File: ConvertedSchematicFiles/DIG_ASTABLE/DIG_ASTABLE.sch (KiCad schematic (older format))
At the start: 11 parts, among them U1 7404, U4 7400

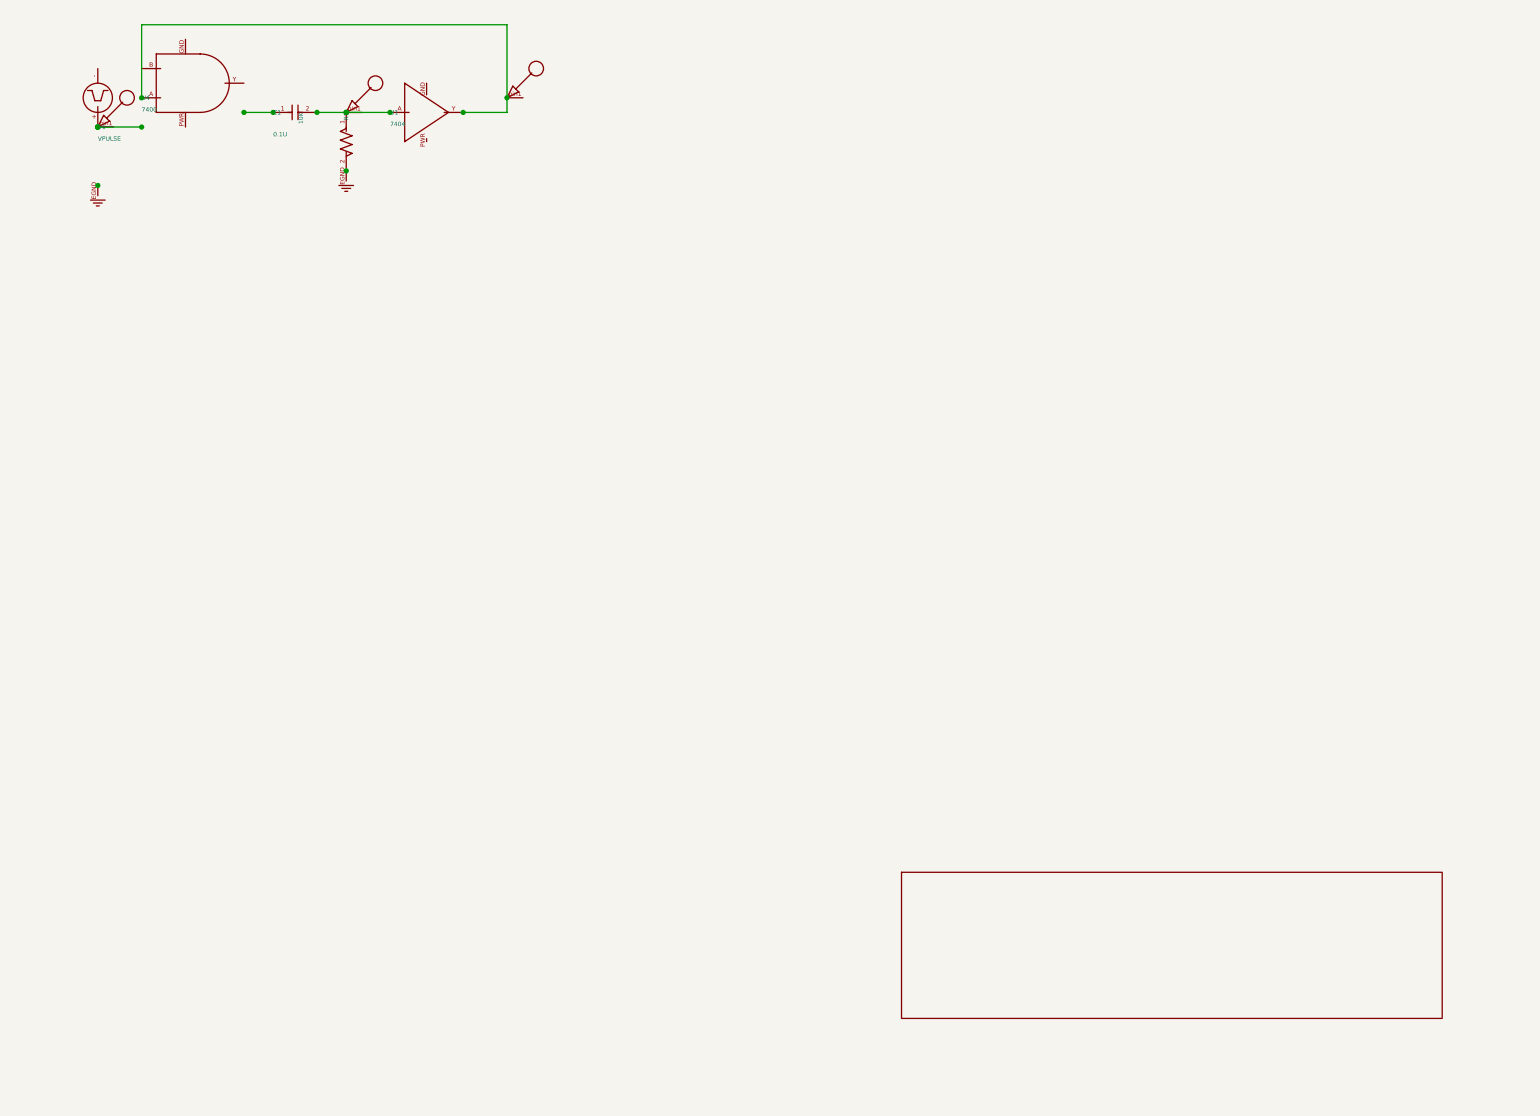
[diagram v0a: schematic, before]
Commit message: Excluded some components. These no longer appear after conversion. When calling shell commands, filenames are in "quotes"
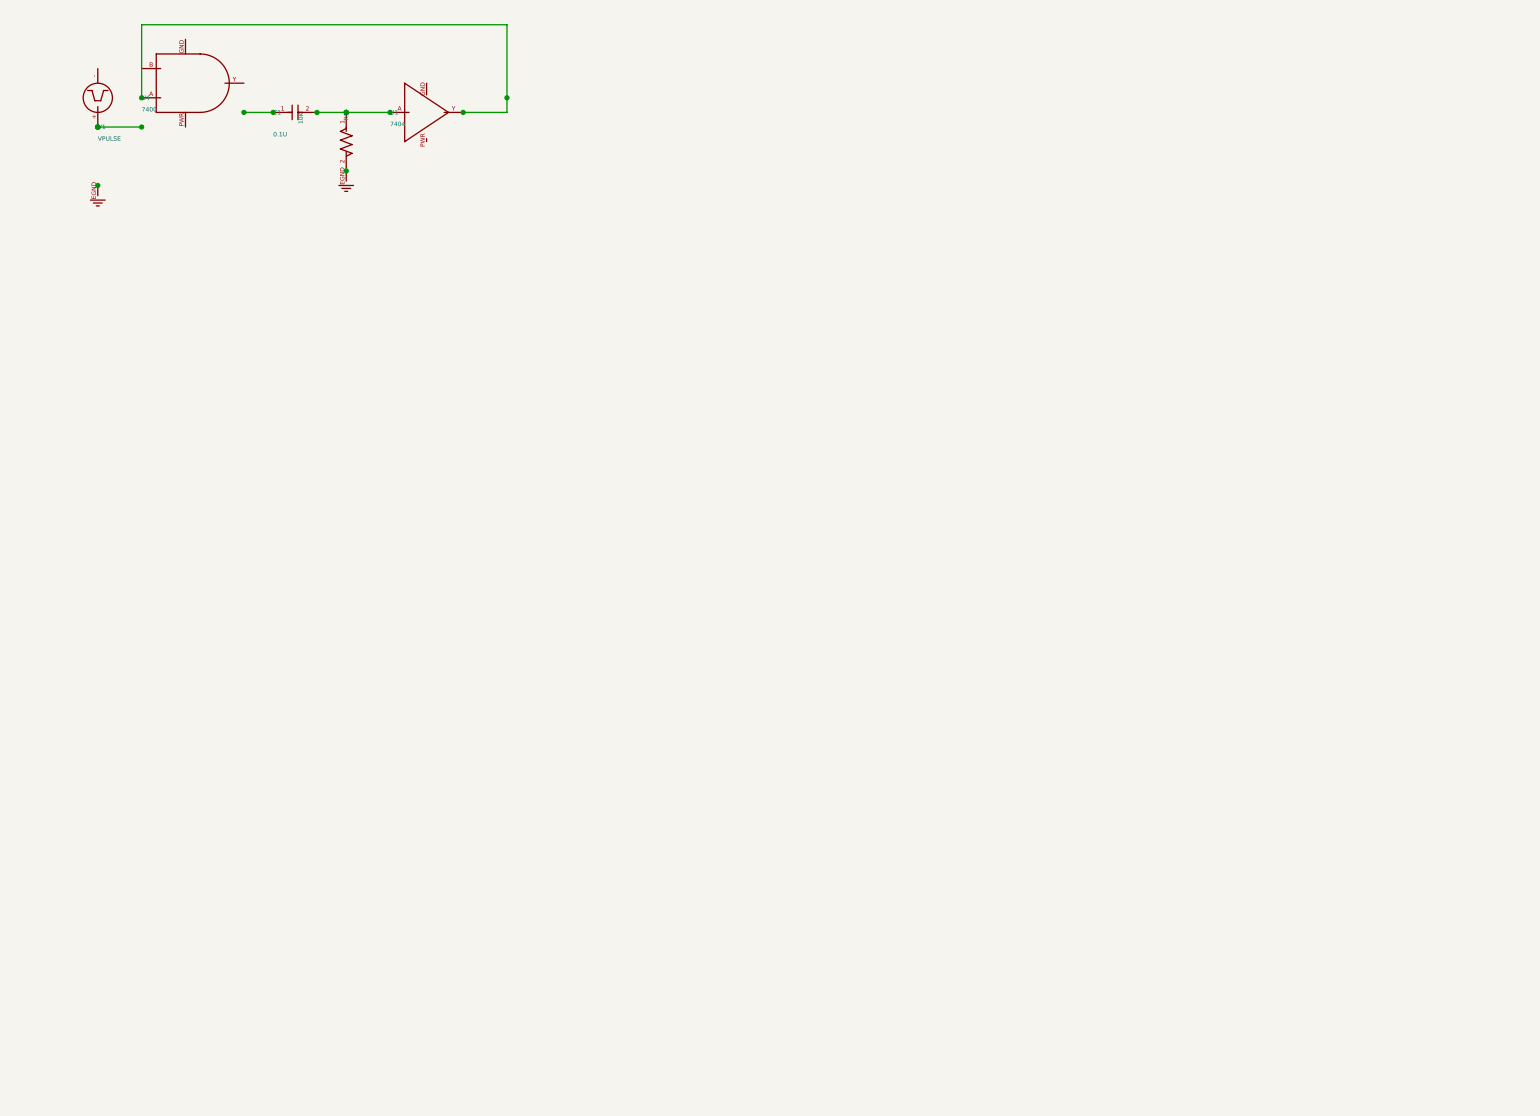
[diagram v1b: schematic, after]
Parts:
- removed nodeMarker (x3): nodeMarker, symbol NODEMARKER_PSPICE
- removed titleblk: titleblk, symbol TITLEBLK_PSPICE
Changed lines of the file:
@@
-	1    0    0    1
-$EndComp
-$Comp
-L TITLEBLK_PSPICE titleblk
-U 1 1 39760492
-P 9700 7200
-F 0 "titleblk" H 19400 14400 30  0001 L CNN
-F 1 "titleblk" H 19400 14480 30  0001 L CNN
-	1    9700 7200
-	1    0    0    1
-$EndComp
-$Comp
-L NODEMARKER_PSPICE nodeMarker
-U 1 1 66516649
-P 3300 900
-F 0 "nodeMarker" H 6600 1800 30  0001 L CNN
-F 1 "nodeMarker" H 6600 1880 30  0001 L CNN
-	1    3300 900
-	1    0    0    1
-$EndComp
-$Comp
-L NODEMARKER_PSPICE nodeMarker
-U 1 1 29641421
-P 2200 1000
-F 0 "nodeMarker" H 4400 2000 30  0001 L CNN
-F 1 "nodeMarker" H 4400 2080 30  0001 L CNN
-	1    2200 1000
-	1    0    0    1
-$EndComp
-$Comp
-L NODEMARKER_PSPICE nodeMarker
-U 1 1 45202362
-P 500 1100
-F 0 "nodeMarker" H 1000 2200 30  0001 L CNN
-F 1 "nodeMarker" H 1000 2280 30  0001 L CNN
-	1    500 1100
 	1    0    0    1
 $EndComp

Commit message: Ports issue fixed. Now annotation for ports is #PWR? function added "itos"
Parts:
- removed EGND (x2): EGND, symbol EGND_PSPICE
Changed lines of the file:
@@
 $EndDescr
 $Comp
-L EGND_PSPICE EGND
+L EGND_PSPICE #PWR1
 U 1 1 14289383
 P 2200 1400
-F 0 "EGND" H 4400 2800 30  0001 L CNN
+F 0 "#PWR1" H 4400 2800 30  0001 L CNN
 F 1 "EGND" H 4400 2880 30  0001 L CNN
 	1    2200 1400
@@
 $EndComp
 $Comp
-L EGND_PSPICE EGND
+L EGND_PSPICE #PWR2
 U 1 1 46930886
 P 500 1500
-F 0 "EGND" H 1000 3000 30  0001 L CNN
+F 0 "#PWR2" H 1000 3000 30  0001 L CNN
 F 1 "EGND" H 1000 3080 30  0001 L CNN
 	1    500 1500

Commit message: Added LICENSE.txt
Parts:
- V1: value VPULSE -> PULSE
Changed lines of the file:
@@
 $EndDescr
 $Comp
-L EGND_PSPICE #PWR1
+L GND #PWR1
 U 1 1 14289383
 P 2200 1400
@@
 $EndComp
 $Comp
-L EGND_PSPICE #PWR2
+L GND #PWR2
 U 1 1 46930886
 P 500 1500
@@
 P 500 1100
 F 0 "V1" H 500 1100 30  0000 L CNN
-F 1 "VPULSE" H 500 1180 30  0000 L CNN
+F 1 "PULSE" H 500 1180 30  0000 L CNN
 	1    500 1100
 	1    0    0    1

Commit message: Orientation fix. Library components are now inverted, with +ve y axis going up. In Schematic files, +ve y axis is downwards. This is how the KiCad libraries are. As a result of the above fixed, the converted GND is now oriented correctly.
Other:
- moved on the sheet: U1, U4, V1
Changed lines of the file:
@@
 F 1 "EGND" H 4400 2880 30  0001 L CNN
 	1    2200 1400
-	1    0    0    1
+	1    0    0    -1
 $EndComp
 $Comp
@@
 F 1 "EGND" H 1000 3080 30  0001 L CNN
 	1    500 1500
-	1    0    0    1
+	1    0    0    -1
 $EndComp
 $Comp
@@
 F 1 "7404" H 2500 1080 30  0000 L CNN
 	1    2500 1000
-	1    0    0    1
+	1    0    0    -1
 $EndComp
 $Comp
@@
 F 1 "7400" H 800 980 30  0000 L CNN
 	1    800 900
-	1    0    0    1
+	1    0    0    -1
 $EndComp
 $Comp
@@
 F 1 "0.1U" H 1700 1150 30  0000 L CNN
 	1    1700 1000
-	1    0    0    1
+	1    0    0    -1
 $EndComp
 $Comp
@@
 F 1 "10K" H 2200 1310 30  0000 L CNN
 	1    2200 1000
-	0    -1    1    0
+	0    1    1    0
 $EndComp
 $Comp
@@
 F 1 "PULSE" H 500 1180 30  0000 L CNN
 	1    500 1100
-	1    0    0    1
+	1    0    0    -1
 $EndComp
 Wire Wire Line

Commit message: Removed the use of exec, wrote basename function, made integration with eSim easier.
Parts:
- added nodeMarker (x3): nodeMarker, symbol nodeMarker_PSPICE
- added titleblk: titleblk, symbol titleblk_PSPICE
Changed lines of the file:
@@
-EESchema Schematic File Version 2  date Sunday 15 August 1999 03:10:25 AM IST
+EESchema Schematic File Version 2  date
 LIBS:power
 LIBS:device
@@
 LIBS:contrib
 LIBS:valves
-LIBS:ConvertedSchematicFiles/DIG_ASTABLE-cache
 EELAYER 25  0
 EELAYER END
@@
 Sheet 1 1
 Title ""
-Date "15 Aug 1999"
+Date ""
 Rev ""
 Comp ""
@@
 	1    500 1100
 	1    0    0    -1
+$EndComp
+$Comp
+L titleblk_PSPICE titleblk
+U 1 1 39760492
+P 9700 7200
+F 0 "titleblk" H 19400 14400 30  0001 L CNN
+F 1 "titleblk" H 19400 14480 30  0001 L CNN
+	1    9700 7200
+	1    0    0    -1
+$EndComp
+$Comp
+L nodeMarker_PSPICE nodeMarker
+U 1 1 66516649
+P 3300 900
+F 0 "nodeMarker" H 6600 1800 30  0001 L CNN
+F 1 "nodeMarker" H 6600 1880 30  0001 L CNN
+	1    3300 900
+	1    0    0    -1
+$EndComp
+$Comp
+L nodeMarker_PSPICE nodeMarker
+U 1 1 29641421
+P 2200 1000
+F 0 "nodeMarker" H 4400 2000 30  0001 L CNN
+F 1 "nodeMarker" H 4400 2080 30  0001 L CNN
+	1    2200 1000
+	1    0    0    -1
+$EndComp
+$Comp
+L nodeMarker_PSPICE nodeMarker
+U 1 1 45202362
+P 500 1100
+F 0 "nodeMarker" H 1000 2200 30  0001 L CNN
+F 1 "nodeMarker" H 1000 2280 30  0001 L CNN
+	1    500 1100
+	1    0    0    -1
